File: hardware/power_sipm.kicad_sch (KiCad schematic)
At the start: 57 parts, among them U24 TPS7A7002DDA, U25 TPS54302, U26 TPS54302, U27 TPS7A7002DDA

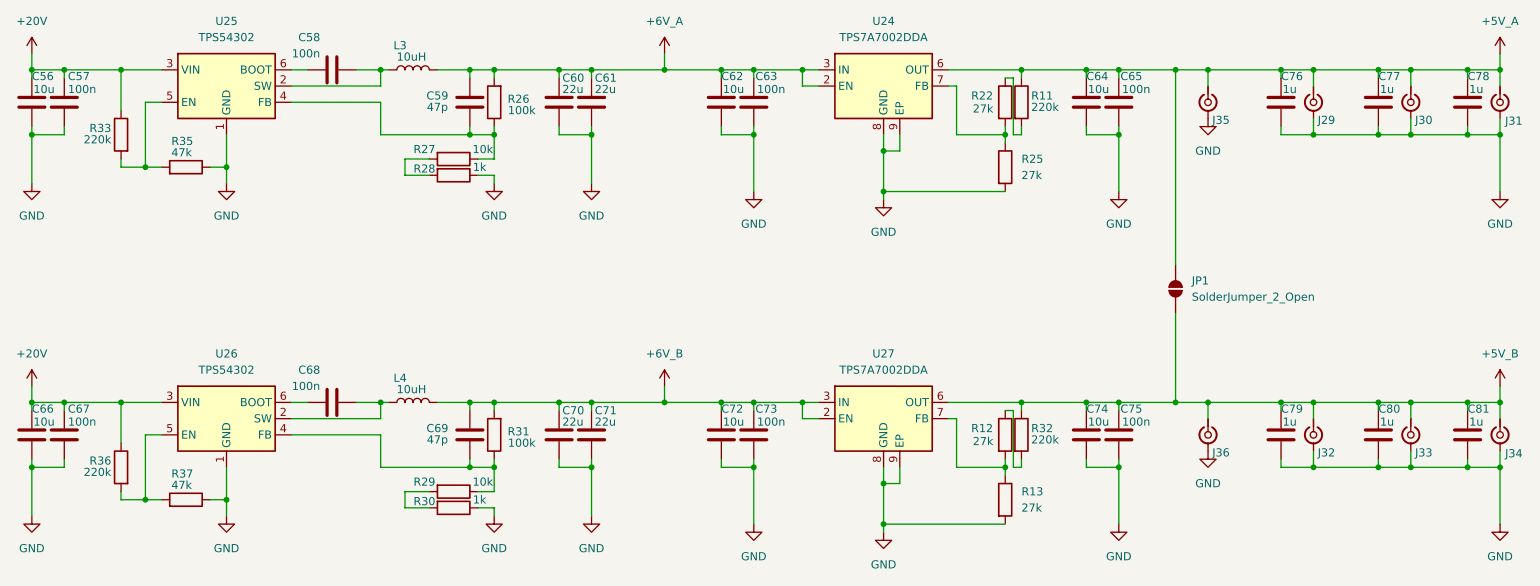
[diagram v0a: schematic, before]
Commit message: complete schematic wiring
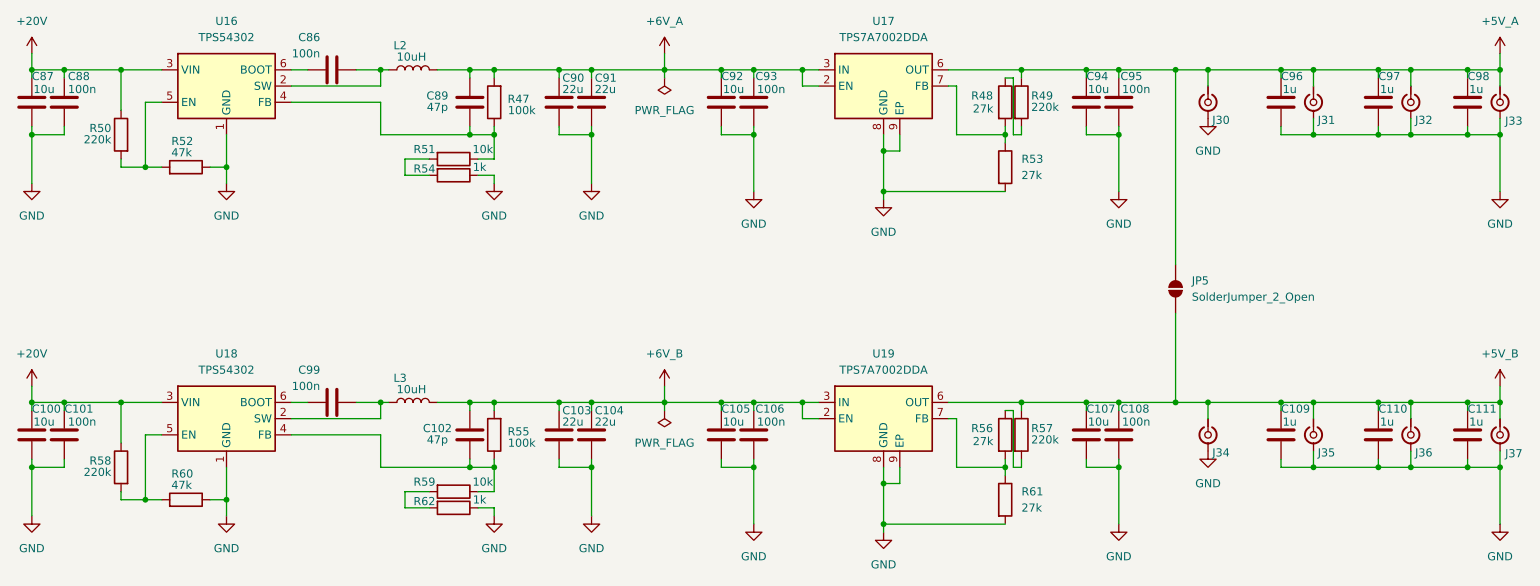
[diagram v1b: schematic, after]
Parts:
- renumbered C66 to C100, C67 to C101, C69 to C102, C70 to C103, C71 to C104, C72 to C105, C73 to C106, C74 to C107, C75 to C108, C79 to C109, C80 to C110, C81 to C111, C58 to C86, C56 to C87, C57 to C88, C59 to C89, C60 to C90, C61 to C91, C62 to C92, C63 to C93, C64 to C94, C65 to C95, C76 to C96, C77 to C97, C78 to C98, C68 to C99, J35 to J30, J29 to J31, J30 to J32, J31 to J33, J36 to J34, J32 to J35, J33 to J36, J34 to J37, JP1 to JP5, L3 to L2, L4 to L3, R26 to R47, R22 to R48, R11 to R49, R33 to R50, R27 to R51, R35 to R52, R25 to R53, R28 to R54, R31 to R55, R12 to R56, R32 to R57, R36 to R58, R29 to R59, R37 to R60, R13 to R61, R30 to R62, U25 to U16, U24 to U17, U26 to U18, U27 to U19

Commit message: update power system + add LCSC part numbers
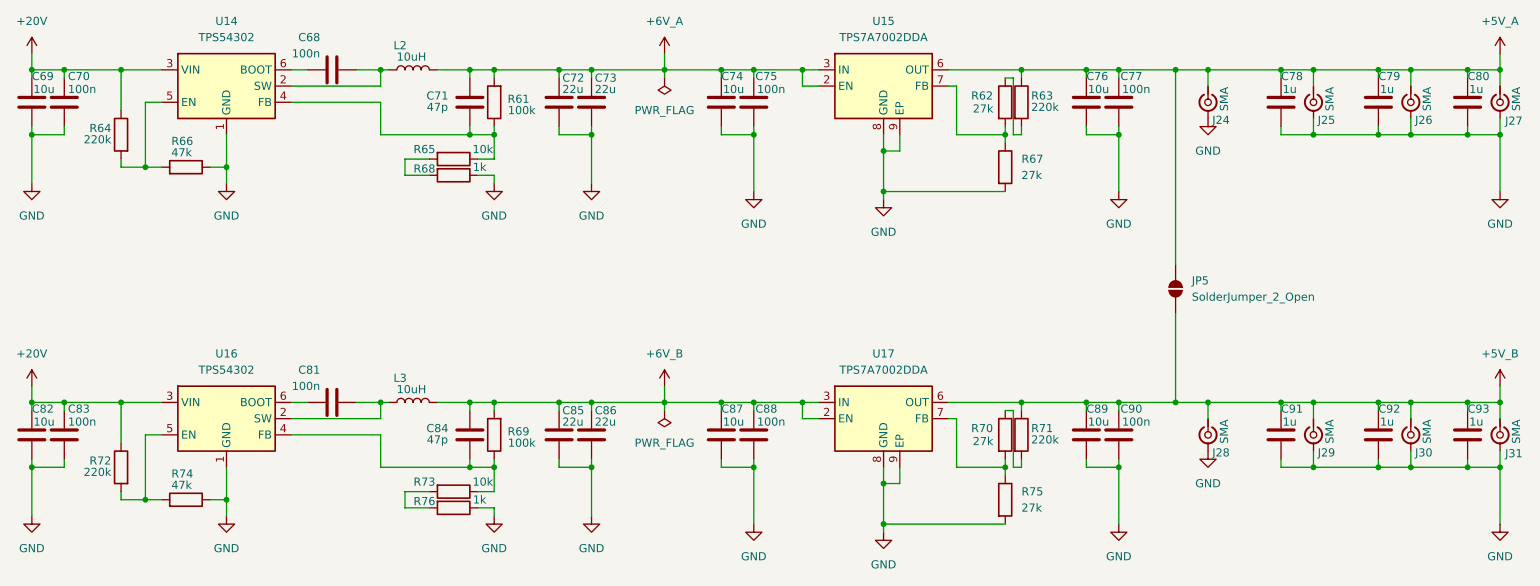
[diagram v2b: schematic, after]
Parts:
- C75: renamed from C93; footprint (none) -> Capacitor_SMD:C_0402_1005Metric; LCSC (none) -> C307331
- C77: renamed from C95; footprint (none) -> Capacitor_SMD:C_0402_1005Metric; LCSC (none) -> C307331
- C78: renamed from C96; footprint Capacitor_SMD:C_1206_3216Metric -> Capacitor_SMD:C_0805_2012Metric; LCSC C13585 -> C28323
- C79: renamed from C97; footprint Capacitor_SMD:C_1206_3216Metric -> Capacitor_SMD:C_0805_2012Metric; LCSC C13585 -> C28323
- C80: renamed from C98; footprint Capacitor_SMD:C_1206_3216Metric -> Capacitor_SMD:C_0805_2012Metric; LCSC C13585 -> C28323
- C88: renamed from C106; footprint (none) -> Capacitor_SMD:C_0402_1005Metric; LCSC (none) -> C307331
- C90: renamed from C108; footprint (none) -> Capacitor_SMD:C_0402_1005Metric; LCSC (none) -> C307331
- C91: renamed from C109; footprint Capacitor_SMD:C_1206_3216Metric -> Capacitor_SMD:C_0805_2012Metric; LCSC C13585 -> C28323
- C92: renamed from C110; footprint Capacitor_SMD:C_1206_3216Metric -> Capacitor_SMD:C_0805_2012Metric; LCSC C13585 -> C28323
- C93: renamed from C111; footprint Capacitor_SMD:C_1206_3216Metric -> Capacitor_SMD:C_0805_2012Metric; LCSC C13585 -> C28323
- J24: renamed from J30; value ~ -> SMA; footprint (none) -> Connector_Coaxial:SMA_Amphenol_901-144_Vertical
- J25: renamed from J31; value ~ -> SMA; footprint (none) -> Connector_Coaxial:SMA_Amphenol_901-144_Vertical
- J26: renamed from J32; value ~ -> SMA; footprint (none) -> Connector_Coaxial:SMA_Amphenol_901-144_Vertical
- J27: renamed from J33; value ~ -> SMA; footprint (none) -> Connector_Coaxial:SMA_Amphenol_901-144_Vertical
- J28: renamed from J34; value ~ -> SMA; footprint (none) -> Connector_Coaxial:SMA_Amphenol_901-144_Vertical
- J29: renamed from J35; value ~ -> SMA; footprint (none) -> Connector_Coaxial:SMA_Amphenol_901-144_Vertical
- J30: renamed from J36; value ~ -> SMA; footprint (none) -> Connector_Coaxial:SMA_Amphenol_901-144_Vertical
- J31: renamed from J37; value ~ -> SMA; footprint (none) -> Connector_Coaxial:SMA_Amphenol_901-144_Vertical
- JP5: footprint (none) -> Jumper:SolderJumper-2_P1.3mm_Open_RoundedPad1.0x1.5mm
- L2, L3: footprint Inductor_SMD:L_Changjiang_FXL0530 -> Inductor_SMD:L_Changjiang_FXL0630; LCSC C177248 -> C167223
- R62: renamed from R48; footprint (none) -> Resistor_SMD:R_0603_1608Metric; LCSC (none) -> C22967
- R63: renamed from R49; footprint (none) -> Resistor_SMD:R_0603_1608Metric; LCSC (none) -> C22961
- R64: renamed from R50; footprint (none) -> Resistor_SMD:R_0603_1608Metric; LCSC (none) -> C22961
- R65: renamed from R51; LCSC C25768 -> C25744
- R66: renamed from R52; footprint (none) -> Resistor_SMD:R_0402_1005Metric; LCSC (none) -> C25792
- R67: renamed from R53; footprint (none) -> Resistor_SMD:R_0603_1608Metric; LCSC (none) -> C22967
- R68: renamed from R54; LCSC C25768 -> C11702
- R70: renamed from R56; footprint (none) -> Resistor_SMD:R_0603_1608Metric; LCSC (none) -> C22967
- R71: renamed from R57; footprint (none) -> Resistor_SMD:R_0603_1608Metric; LCSC (none) -> C22961
- R72: renamed from R58; footprint (none) -> Resistor_SMD:R_0603_1608Metric; LCSC (none) -> C22961
- R73: renamed from R59; LCSC C25768 -> C25744
- R74: renamed from R60; footprint (none) -> Resistor_SMD:R_0402_1005Metric; LCSC (none) -> C25792
- R75: renamed from R61; footprint (none) -> Resistor_SMD:R_0603_1608Metric; LCSC (none) -> C22967
- R76: renamed from R62; LCSC C25768 -> C11702
- U14: renamed from U16; LCSC (none) -> C129370
- U15: renamed from U17; LCSC (none) -> C140311
- U16: renamed from U18; LCSC (none) -> C129370
- U17: renamed from U19; LCSC (none) -> C140311
- renumbered C86 to C68, C87 to C69, C88 to C70, C89 to C71, C90 to C72, C91 to C73, C92 to C74, C94 to C76, C99 to C81, C100 to C82, C101 to C83, C102 to C84, C103 to C85, C104 to C86, C105 to C87, C107 to C89, R47 to R61, R55 to R69

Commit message: apply manufacturing BOM
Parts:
- renumbered C68 to C72, C69 to C73, C70 to C74, C71 to C75, C72 to C76, C73 to C77, C74 to C78, C75 to C79, C76 to C80, C77 to C81, C78 to C82, C79 to C83, C80 to C84, C81 to C85, C82 to C86, C83 to C87, C84 to C88, C85 to C89, C86 to C90, C87 to C91, C88 to C92, C89 to C93, C90 to C94, C91 to C95, C92 to C96, C93 to C97, J24 to J23, J25 to J24, J26 to J25, J27 to J26, J28 to J27, J29 to J28, J30 to J29, J31 to J30, L2 to L4, L3 to L5, R61 to R69, R62 to R70, R63 to R71, R64 to R72, R65 to R73, R66 to R74, R67 to R75, R68 to R76, R69 to R77, R70 to R78, R71 to R79, R72 to R80, R73 to R81, R74 to R82, R75 to R83, R76 to R84

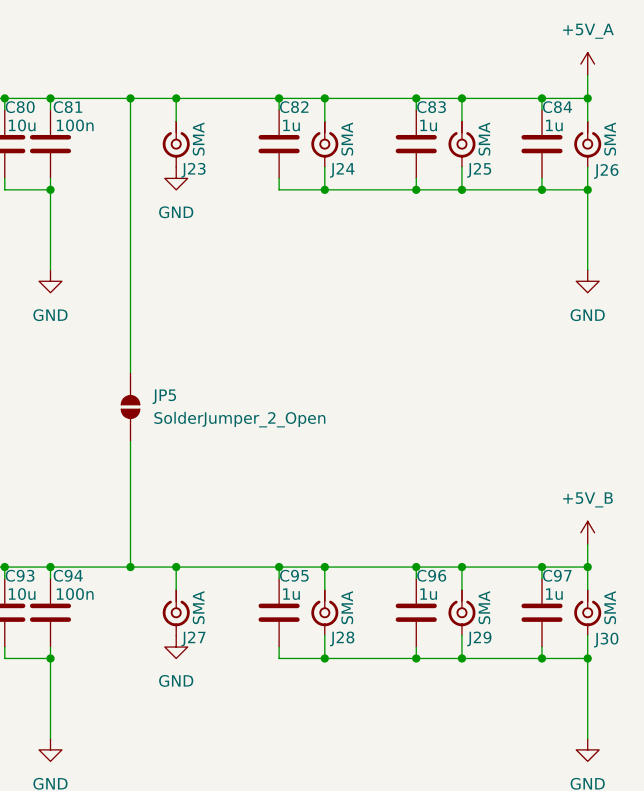
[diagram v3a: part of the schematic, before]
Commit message: route digital inputs
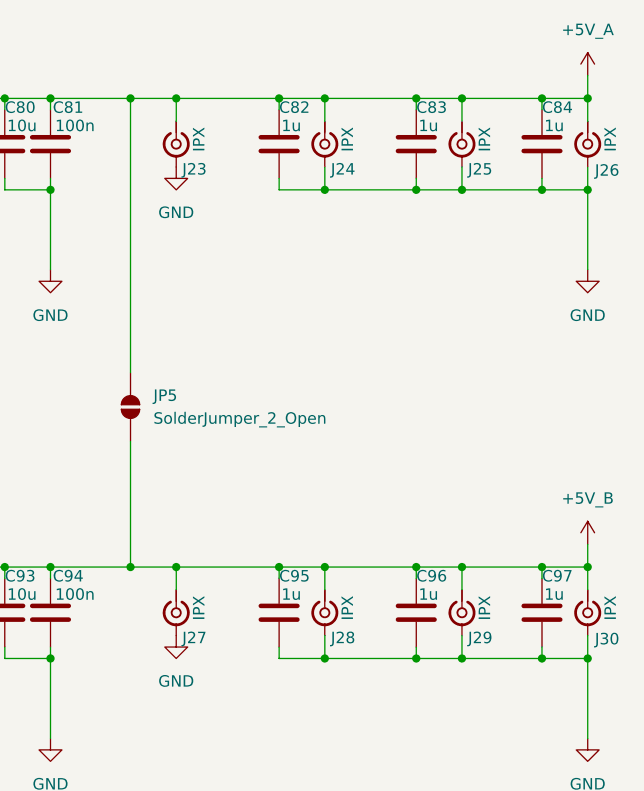
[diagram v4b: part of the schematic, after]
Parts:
- J23, J24, J25, J26, J27, J28, J29, J30: value SMA -> IPX; footprint Connector_Coaxial:SMA_Amphenol_901-144_Vertical -> digital:BWIPX-1-001E
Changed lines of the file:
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@@
 			)
 		)
-		(property "Value" "SMA"
+		(property "Value" "IPX"
 			(at 250.19 59.1704 0)
 			(effects
@@
 			)
 		)
-		(property "Footprint" "Connector_Coaxial:SMA_Amphenol_901-144_Vertical"
+		(property "Footprint" "digital:BWIPX-1-001E"
 			(at 247.65 59.69 0)
 			(effects
@@
 			)
 		)
-		(property "Value" "SMA"
+		(property "Value" "IPX"
 			(at 218.44 59.1704 0)
 			(effects
@@
 			)
 		)
-		(property "Footprint" "Connector_Coaxial:SMA_Amphenol_901-144_Vertical"
+		(property "Footprint" "digital:BWIPX-1-001E"
 			(at 215.9 59.69 0)
 			(effects
@@
 			)
 		)
-		(property "Value" "SMA"
+		(property "Value" "IPX"
 			(at 250.19 111.2404 0)
 			(effects
@@
 			)
 		)
-		(property "Footprint" "Connector_Coaxial:SMA_Amphenol_901-144_Vertical"
+		(property "Footprint" "digital:BWIPX-1-001E"
 			(at 247.65 111.76 0)
 			(effects
@@
 			)
 		)
-		(property "Value" "SMA"
+		(property "Value" "IPX"
 			(at 264.16 59.1704 0)
 			(effects
@@
 			)
 		)
-		(property "Footprint" "Connector_Coaxial:SMA_Amphenol_901-144_Vertical"
+		(property "Footprint" "digital:BWIPX-1-001E"
 			(at 261.62 59.69 0)
 			(effects
@@
 			)
 		)
-		(property "Value" "SMA"
+		(property "Value" "IPX"
 			(at 218.44 111.2404 0)
 			(effects
@@
 			)
 		)
-		(property "Footprint" "Connector_Coaxial:SMA_Amphenol_901-144_Vertical"
+		(property "Footprint" "digital:BWIPX-1-001E"
 			(at 215.9 111.76 0)
 			(effects
@@
 			)
 		)
-		(property "Value" "SMA"
+		(property "Value" "IPX"
 			(at 234.95 59.1704 0)
 			(effects
@@
 			)
 		)
-		(property "Footprint" "Connector_Coaxial:SMA_Amphenol_901-144_Vertical"
+		(property "Footprint" "digital:BWIPX-1-001E"
 			(at 232.41 59.69 0)
 			(effects
@@
 			)
 		)
-		(property "Value" "SMA"
+		(property "Value" "IPX"
 			(at 264.16 111.2404 0)
 			(effects
@@
 			)
 		)
-		(property "Footprint" "Connector_Coaxial:SMA_Amphenol_901-144_Vertical"
+		(property "Footprint" "digital:BWIPX-1-001E"
 			(at 261.62 111.76 0)
 			(effects
@@
 			)
 		)
-		(property "Value" "SMA"
+		(property "Value" "IPX"
 			(at 234.95 111.2404 0)
 			(effects
@@
 			)
 		)
-		(property "Footprint" "Connector_Coaxial:SMA_Amphenol_901-144_Vertical"
+		(property "Footprint" "digital:BWIPX-1-001E"
 			(at 232.41 111.76 0)
 			(effects

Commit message: route more
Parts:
- J23, J24, J25, J26, J27, J28, J29, J30: value IPX -> IPEX-1; LCSC (none) -> C496552
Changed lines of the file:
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@@
 			)
 		)
-		(property "Value" "IPX"
+		(property "Value" "IPEX-1"
 			(at 250.19 59.1704 0)
 			(effects
@@
 			)
 		)
+		(property "LCSC" "C496552"
+			(at 247.65 59.69 90)
+			(effects
+				(font
+					(size 1.27 1.27)
+				)
+				(hide yes)
+			)
+		)
 		(pin "1"
 		)
@@
 			)
 		)
-		(property "Value" "IPX"
+		(property "Value" "IPEX-1"
 			(at 218.44 59.1704 0)
 			(effects
@@
 			)
 		)
+		(property "LCSC" "C496552"
+			(at 215.9 59.69 90)
+			(effects
+				(font
+					(size 1.27 1.27)
+				)
+				(hide yes)
+			)
+		)
 		(pin "1"
 		)
@@
 			)
 		)
-		(property "Value" "IPX"
+		(property "Value" "IPEX-1"
 			(at 250.19 111.2404 0)
 			(effects
@@
 			)
 		)
+		(property "LCSC" "C496552"
+			(at 247.65 111.76 90)
+			(effects
+				(font
+					(size 1.27 1.27)
+				)
+				(hide yes)
+			)
+		)
 		(pin "1"
 		)
@@
 			)
 		)
-		(property "Value" "IPX"
+		(property "Value" "IPEX-1"
 			(at 264.16 59.1704 0)
 			(effects
@@
 			)
 		)
+		(property "LCSC" "C496552"
+			(at 261.62 59.69 90)
+			(effects
+				(font
+					(size 1.27 1.27)
+				)
+				(hide yes)
+			)
+		)
 		(pin "1"
 		)
@@
 			)
 		)
-		(property "Value" "IPX"
+		(property "Value" "IPEX-1"
 			(at 218.44 111.2404 0)
 			(effects
@@
 			)
 		)
+		(property "LCSC" "C496552"
+			(at 215.9 111.76 90)
+			(effects
+				(font
+					(size 1.27 1.27)
+				)
+				(hide yes)
+			)
+		)
 		(pin "1"
 		)
@@
 			)
 		)
-		(property "Value" "IPX"
+		(property "Value" "IPEX-1"
 			(at 234.95 59.1704 0)
 			(effects
@@
 			)
 		)
+		(property "LCSC" "C496552"
+			(at 232.41 59.69 90)
+			(effects
+				(font
+					(size 1.27 1.27)
+				)
+				(hide yes)
+			)
+		)
 		(pin "1"
 		)
@@
 			)
 		)
-		(property "Value" "IPX"
+		(property "Value" "IPEX-1"
 			(at 264.16 111.2404 0)
 			(effects
@@
 			)
 		)
+		(property "LCSC" "C496552"
+			(at 261.62 111.76 90)
+			(effects
+				(font
+					(size 1.27 1.27)
+				)
+				(hide yes)
+			)
+		)
 		(pin "1"
 		)
@@
 			)
 		)
-		(property "Value" "IPX"
+		(property "Value" "IPEX-1"
 			(at 234.95 111.2404 0)
 			(effects
@@
 			(effects
 				(font
+					(size 1.27 1.27)
+				)
+				(hide yes)
+			)
+		)
+		(property "LCSC" "C496552"
+			(at 232.41 111.76 90)
+			(effects
+				(font
